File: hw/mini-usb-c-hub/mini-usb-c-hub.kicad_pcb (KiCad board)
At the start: 4 copper layers, 56 x 30 mm, 46 parts, among them J101 USB_C_Receptacle_USB2.0_16P, J201 USB_C_Receptacle_USB2.0_16P, J301 USB_C_Receptacle_USB2.0_16P, J401 USB_A, J501 USB_A, U101 FE1.1s, Y101 12MHz

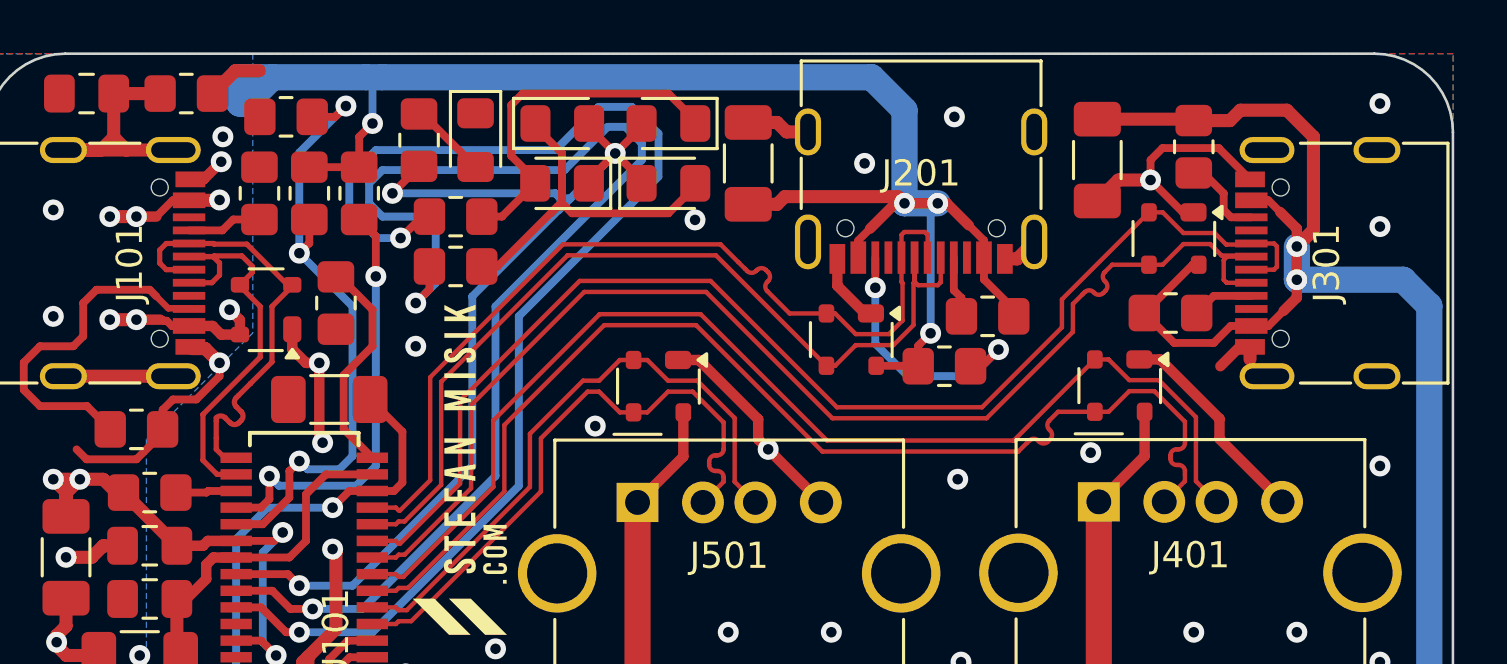
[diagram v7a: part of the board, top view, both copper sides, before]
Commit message: refactor(hw): layout improvements
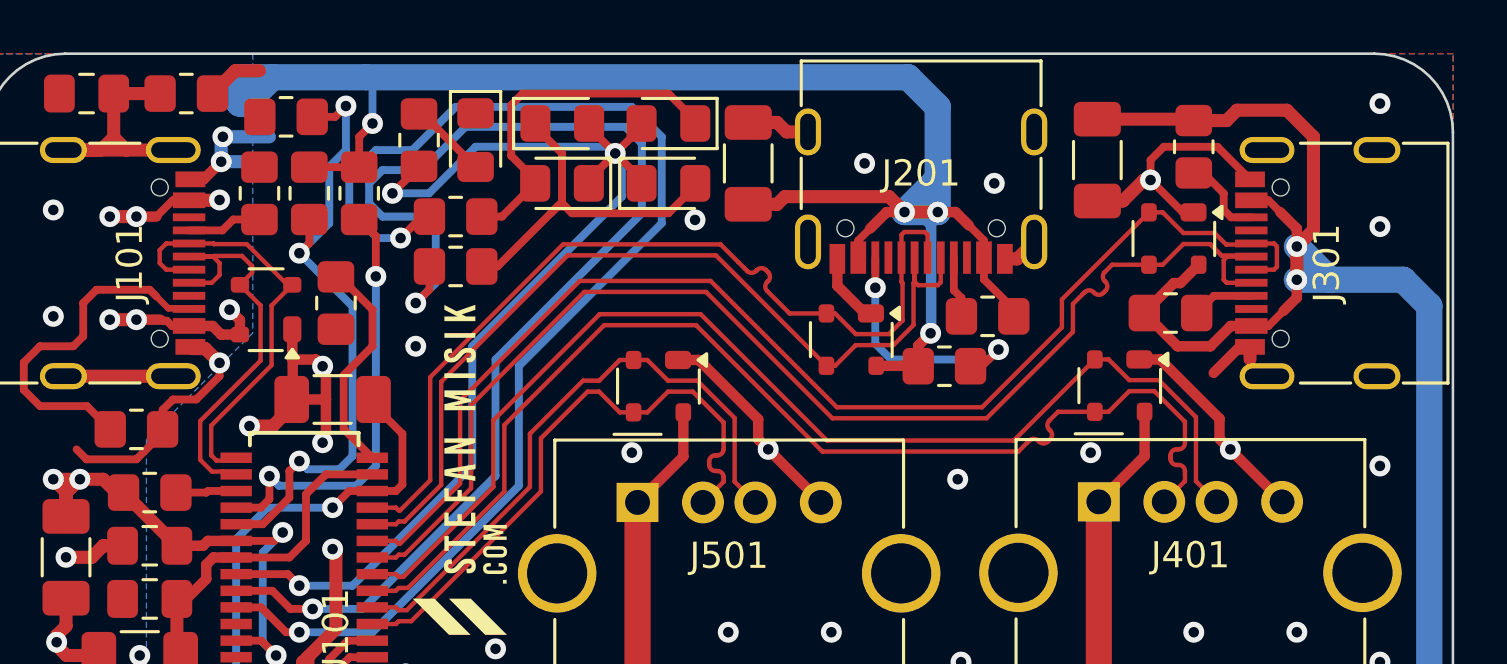
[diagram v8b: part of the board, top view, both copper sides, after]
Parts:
- moved C108 0.13 mm to (127.5, 102.1)
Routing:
- net GND: track 96.6 -> 107.0 mm, vias 41 -> 43
- net +5V: track 209.5 -> 215.8 mm
- net /DRV: track 40.9 -> 42.5 mm
- net /UUSB-: track 17.0 -> 16.4 mm
- net Net-(J201-CC2): track 10.3 -> 9.73 mm
